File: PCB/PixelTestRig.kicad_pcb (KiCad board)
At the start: 2 copper layers, 115 x 40 mm, 30 parts, among them J1 RPi_GPIO, J2 GS2, P0 STRIP_OUT, P1 STRIP_OUT, P2 STRIP_OUT, P3 STRIP_OUT, P4 STRIP_OUT, P5 STRIP_OUT, P6 APM_INPUT, Q0 IRLB8721PBF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

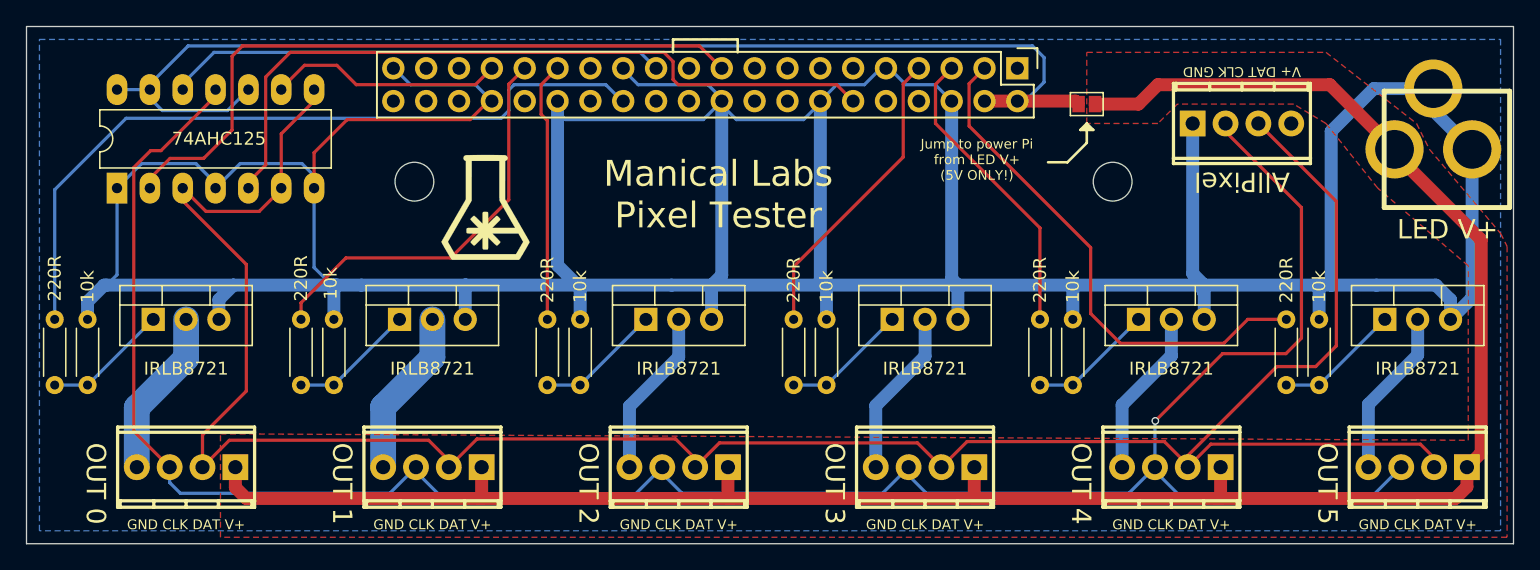
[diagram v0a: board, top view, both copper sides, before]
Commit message: Updated CvPcb
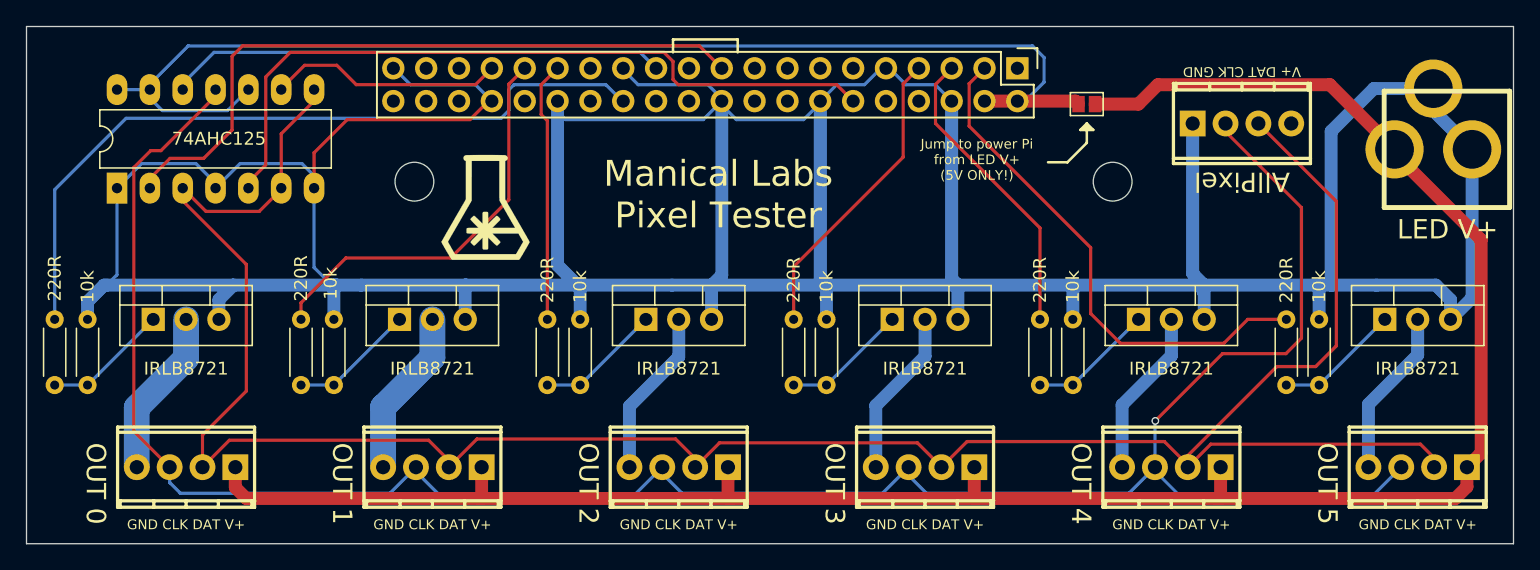
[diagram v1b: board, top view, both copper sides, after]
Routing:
- removed copper zone on B.Cu, net GND
- removed copper zone on F.Cu, net PWR
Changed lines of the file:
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@@
     (links 81)
     (no_connects 0)
-    (area 40.949999 97.949999 156.050001 138.050001)
+    (area 40.949999 96.525 158.255809 138.15248)
     (thickness 1.6)
     (drawings 41)
@@
   (page A4)
   (layers
-    (0 F.Cu signal hide)
-    (31 B.Cu signal hide)
+    (0 F.Cu signal)
+    (31 B.Cu signal)
     (34 B.Paste user)
     (35 F.Paste user)
@@
   (segment (start 138.43 125.73) (end 140.97 125.73) (width 0.25) (layer B.Cu) (net 48))
   (segment (start 140.97 125.73) (end 146.05 120.65) (width 0.25) (layer B.Cu) (net 48))
-  (zone (net 20) (net_name GND) (layer B.Cu) (hatch edge 0.508)
-    (connect_pads (clearance 0.508))
-    (min_thickness 0.254)
-    (fill yes (arc_segments 16) (thermal_gap 0.508) (thermal_bridge_width 0.508))
-    (polygon
-      (pts
-        (xy 155 137) (xy 42 137) (xy 42 99) (xy 155 99)
-      )
-    )
-  )
-  (zone (net 19) (net_name PWR) (layer F.Cu) (hatch edge 0.508)
-    (connect_pads (clearance 0.508))
-    (min_thickness 0.254)
-    (fill yes (arc_segments 16) (thermal_gap 0.508) (thermal_bridge_width 0.508))
-    (polygon
-      (pts
-        (xy 148.5 105.5) (xy 149.5 107.5) (xy 155 114) (xy 155.5 115) (xy 155.5 137.5)
-        (xy 56 137.5) (xy 56 129.5) (xy 152.5 130) (xy 152.5 116.5) (xy 145.5 110.5)
-        (xy 141.5 105.5) (xy 139 104) (xy 130 104) (xy 128.5 105.5) (xy 123 105.5)
-        (xy 123 100) (xy 141.5 100)
-      )
-    )
-  )
 )

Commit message: layout redone with PNP
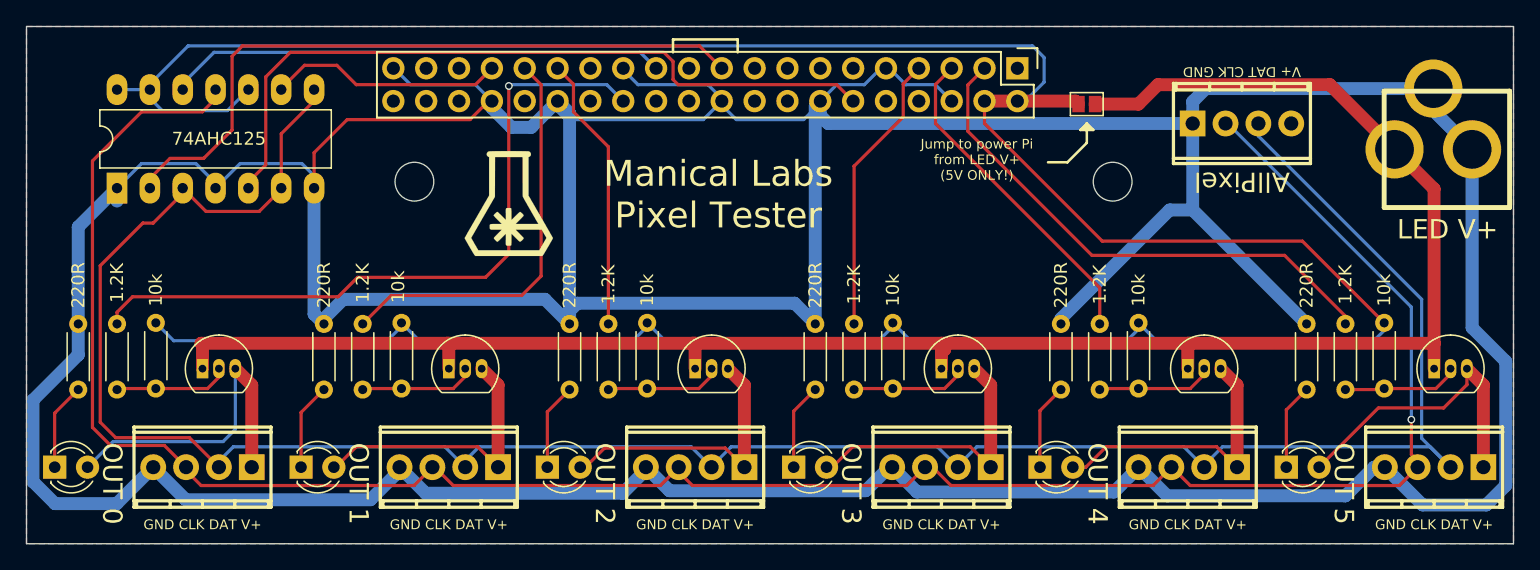
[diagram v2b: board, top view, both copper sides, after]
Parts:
- added D0: LED, LEDs:LED_D3.0mm, F.Cu at (138.4, 132.1)
- added D1: LED, LEDs:LED_D3.0mm, F.Cu at (119.4, 132.1)
- added D2: LED, LEDs:LED_D3.0mm, F.Cu at (100.3, 132.1)
- added D3: LED, LEDs:LED_D3.0mm, F.Cu at (81.3, 132.1)
- added D4: LED, LEDs:LED_D3.0mm, F.Cu at (62.2, 132.1)
- added D5: LED, LEDs:LED_D3.0mm, F.Cu at (43.2, 132.1)
- added R12: 220R, Resistors_THT:R_Axial_DIN0204_L3.6mm_D1.6mm_P5.08mm_Horizontal, F.Cu at (45.0, 121.0)
- added R13: 220R, Resistors_THT:R_Axial_DIN0204_L3.6mm_D1.6mm_P5.08mm_Horizontal, F.Cu at (64.0, 121.0)
- added R14: 220R, Resistors_THT:R_Axial_DIN0204_L3.6mm_D1.6mm_P5.08mm_Horizontal, F.Cu at (83.0, 121.0)
- added R15: 220R, Resistors_THT:R_Axial_DIN0204_L3.6mm_D1.6mm_P5.08mm_Horizontal, F.Cu at (102.0, 121.0)
- added R16: 220R, Resistors_THT:R_Axial_DIN0204_L3.6mm_D1.6mm_P5.08mm_Horizontal, F.Cu at (121.0, 121.0)
- added R17: 220R, Resistors_THT:R_Axial_DIN0204_L3.6mm_D1.6mm_P5.08mm_Horizontal, F.Cu at (140.0, 121.0)
- Q0, Q1, Q2, Q3, Q4, Q5: value IRLB8721PBF -> PN2907BU; footprint TO_SOT_Packages_THT:TO-220-3_Vertical -> TO_SOT_Packages_THT:TO-92_Inline_Narrow_Oval
- R10, R11, R6, R7, R8, R9: value 220R -> 1.2K
- moved Q0 99.1 mm to (149.9, 124.5)
- moved Q5 91.5 mm to (54.6, 124.5)
- moved Q1 61.1 mm to (130.8, 124.5)
- moved Q4 53.5 mm to (73.7, 124.5)
- moved Q2 23.2 mm to (111.8, 124.5)
- moved Q3 15.7 mm to (92.7, 124.5)
- moved R0 5.29 mm to (51.0, 126.0)
- moved R1 5.24 mm to (70.0, 126.0)
- moved R2 5.19 mm to (89.0, 126.0)
- moved R3 5.14 mm to (108.0, 126.0)
- moved R4 5.09 mm to (127.0, 126.0)
- moved R5 5.04 mm to (146.0, 126.0)
- moved R6 4.83 mm to (48.0, 121.0)
- moved R7 4.78 mm to (67.0, 121.0)
- moved R8 4.73 mm to (86.0, 121.0)
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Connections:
- P0 pad 1: PWR -> Net-(D5-Pad2)
- P0 pad 4: Net-(P0-Pad4) -> GND
- P1 pad 1: PWR -> Net-(D4-Pad2)
- P1 pad 4: Net-(P1-Pad4) -> GND
- P2 pad 1: PWR -> Net-(D3-Pad2)
- P2 pad 4: Net-(P2-Pad4) -> GND
- P3 pad 1: PWR -> Net-(D2-Pad2)
- P3 pad 4: Net-(P3-Pad4) -> GND
- P4 pad 1: PWR -> Net-(D1-Pad2)
- P4 pad 4: Net-(P4-Pad4) -> GND
- P5 pad 1: PWR -> Net-(D0-Pad2)
- P5 pad 4: Net-(P5-Pad4) -> GND
- Q0 pad 1: Net-(Q0-Pad1) -> PWR
- Q0 pad 2: Net-(P0-Pad4) -> Net-(Q0-Pad2)
- Q0 pad 3: GND -> Net-(D0-Pad2)
- Q1 pad 1: Net-(Q1-Pad1) -> PWR
- Q1 pad 2: Net-(P1-Pad4) -> Net-(Q1-Pad2)
- Q1 pad 3: GND -> Net-(D1-Pad2)
- Q2 pad 1: Net-(Q2-Pad1) -> PWR
- Q2 pad 2: Net-(P2-Pad4) -> Net-(Q2-Pad2)
- Q2 pad 3: GND -> Net-(D2-Pad2)
- Q3 pad 1: Net-(Q3-Pad1) -> PWR
- Q3 pad 2: Net-(P3-Pad4) -> Net-(Q3-Pad2)
- Q3 pad 3: GND -> Net-(D3-Pad2)
- Q4 pad 1: Net-(Q4-Pad1) -> PWR
- Q4 pad 2: Net-(P4-Pad4) -> Net-(Q4-Pad2)
- Q4 pad 3: GND -> Net-(D4-Pad2)
- Q5 pad 1: Net-(Q5-Pad1) -> PWR
- Q5 pad 2: Net-(P5-Pad4) -> Net-(Q5-Pad2)
- Q5 pad 3: GND -> Net-(D5-Pad2)
- R0 pad 1: Net-(Q0-Pad1) -> Net-(Q5-Pad2)
- R0 pad 2: GND -> 5V
- R1 pad 1: Net-(Q1-Pad1) -> Net-(Q4-Pad2)
- R1 pad 2: GND -> 5V
- R10 pad 2: Net-(Q4-Pad1) -> Net-(Q1-Pad2)
- R11 pad 2: Net-(Q5-Pad1) -> Net-(Q0-Pad2)
- R2 pad 1: Net-(Q2-Pad1) -> Net-(Q3-Pad2)
- R2 pad 2: GND -> 5V
- R3 pad 1: Net-(Q3-Pad1) -> Net-(Q2-Pad2)
- R3 pad 2: GND -> 5V
- R4 pad 1: Net-(Q4-Pad1) -> Net-(Q1-Pad2)
- R4 pad 2: GND -> 5V
- R5 pad 1: Net-(Q5-Pad1) -> Net-(Q0-Pad2)
- R5 pad 2: GND -> 5V
- R6 pad 2: Net-(Q0-Pad1) -> Net-(Q5-Pad2)
- R7 pad 2: Net-(Q1-Pad1) -> Net-(Q4-Pad2)
- R8 pad 2: Net-(Q2-Pad1) -> Net-(Q3-Pad2)
- R9 pad 2: Net-(Q3-Pad1) -> Net-(Q2-Pad2)
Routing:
- net 5V: track 95.0 -> 235.9 mm
- net GND: track 357.5 -> 456.2 mm
- net Net-(D5-Pad2): track 0.00 -> 25.8 mm
- net Net-(D0-Pad2): track 0.00 -> 23.5 mm
- net Net-(D1-Pad2): track 0.00 -> 22.2 mm
- net Net-(D4-Pad2): track 0.00 -> 22.2 mm
- net Net-(D2-Pad2): track 0.00 -> 22.2 mm
- net Net-(D3-Pad2): track 0.00 -> 22.1 mm
- net Net-(P5-Pad4): track 13.0 -> 0.00 mm
- net Net-(P2-Pad4): track 13.0 -> 0.00 mm
- net Net-(P1-Pad4): track 13.0 -> 0.00 mm
- net Net-(P0-Pad4): track 13.0 -> 0.00 mm
- net Net-(P3-Pad4): track 13.0 -> 0.00 mm
- net Net-(P4-Pad4): track 13.0 -> 0.00 mm
- net PWR: track 163.4 -> 151.2 mm
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- added copper zone on B.Cu, net GND
- added copper zone on F.Cu, net PWR
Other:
- board text removed: "IRLB8721"
